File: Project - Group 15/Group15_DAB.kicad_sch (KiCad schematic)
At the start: 41 parts, among them J1 RJ45, J2 RJ45, J3 Power Header

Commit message: swag
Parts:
- FLT: value 100nF -> 22nF
- RIP: value 100nF -> 1nF
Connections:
- new net: R11., R15., R17., U4.2 (IN+)
- new net: R10., R14., R16., U4.3 (IN-)
- new net: R13., R2., R5., U3.3 (IN-)
- new net: R1., R12., R6., U3.2 (IN+)
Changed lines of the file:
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@@
 	)
 	(symbol
-		(lib_name "491_Symbols:RES_1k_805_PAN")
 		(lib_id "491_Symbols:RES_1k_805_PAN")
 		(at 87.63 39.37 270)
@@
 	)
 	(symbol
-		(lib_name "491_Symbols:RES_1k_805_PAN")
 		(lib_id "491_Symbols:RES_1k_805_PAN")
 		(at 53.34 26.67 270)
@@
 	)
 	(symbol
-		(lib_name "491_Symbols:RES_1k_805_PAN")
 		(lib_id "491_Symbols:RES_1k_805_PAN")
 		(at 198.12 118.11 0)
@@
 	)
 	(symbol
-		(lib_name "491_Symbols:RES_1k_805_PAN")
 		(lib_id "491_Symbols:RES_1k_805_PAN")
 		(at 229.87 140.97 0)
@@
 	)
 	(symbol
-		(lib_name "491_Symbols:RES_1k_805_PAN")
 		(lib_id "491_Symbols:RES_1k_805_PAN")
 		(at 142.24 149.86 0)
@@
 	)
 	(symbol
-		(lib_name "491_Symbols:RES_1k_805_PAN")
 		(lib_id "491_Symbols:RES_1k_805_PAN")
 		(at 198.12 128.27 0)
@@
 	)
 	(symbol
-		(lib_name "491_Symbols:RES_1k_805_PAN")
 		(lib_id "491_Symbols:RES_1k_805_PAN")
 		(at 142.24 95.25 0)
@@
 	)
 	(symbol
-		(lib_name "491_Symbols:RES_1k_805_PAN")
 		(lib_id "491_Symbols:RES_1k_805_PAN")
 		(at 231.14 95.25 0)
@@
 	)
 	(symbol
-		(lib_name "491_Symbols:RES_1k_805_PAN")
 		(lib_id "491_Symbols:RES_1k_805_PAN")
 		(at 66.04 26.67 270)
@@
 	)
 	(symbol
-		(lib_name "491_Symbols:RES_1k_805_PAN")
 		(lib_id "491_Symbols:RES_1k_805_PAN")
 		(at 107.95 128.27 0)
@@
 	)
 	(symbol
-		(lib_name "491_Symbols:RES_1k_805_PAN")
 		(lib_id "491_Symbols:RES_1k_805_PAN")
 		(at 142.24 86.36 0)
@@
 	)
 	(symbol
-		(lib_name "491_Symbols:RES_1k_805_PAN")
 		(lib_id "491_Symbols:RES_1k_805_PAN")
 		(at 87.63 26.67 270)
@@
 			)
 		)
-		(property "Value" "100nF"
+		(property "Value" "1nF"
 			(at 173.228 59.436 90)
 			(effects
@@
 	)
 	(symbol
-		(lib_name "491_Symbols:RES_47k_805_PAN")
 		(lib_id "491_Symbols:RES_47k_805_PAN")
 		(at 238.76 44.45 0)
@@
 		)
 		(property "Value" "3k"
-			(at 190.246 66.802 0)
+			(at 190.754 67.056 90)
 			(effects
 				(font
@@
 	)
 	(symbol
-		(lib_name "491_Symbols:RES_1k_805_PAN")
 		(lib_id "491_Symbols:RES_1k_805_PAN")
 		(at 107.95 118.11 0)
@@
 			)
 		)
-		(property "Value" "100nF"
+		(property "Value" "22nF"
 			(at 185.674 56.896 90)
 			(effects
@@
 	)
 	(symbol
-		(lib_name "491_Symbols:RES_1k_805_PAN")
 		(lib_id "491_Symbols:RES_1k_805_PAN")
 		(at 229.87 149.86 0)
@@
 	)
 	(symbol
-		(lib_name "491_Symbols:RES_1k_805_PAN")
 		(lib_id "491_Symbols:RES_1k_805_PAN")
 		(at 231.14 86.36 0)
@@
 	)
 	(symbol
-		(lib_name "491_Symbols:RES_1k_805_PAN")
 		(lib_id "491_Symbols:RES_1k_805_PAN")
 		(at 142.24 140.97 0)

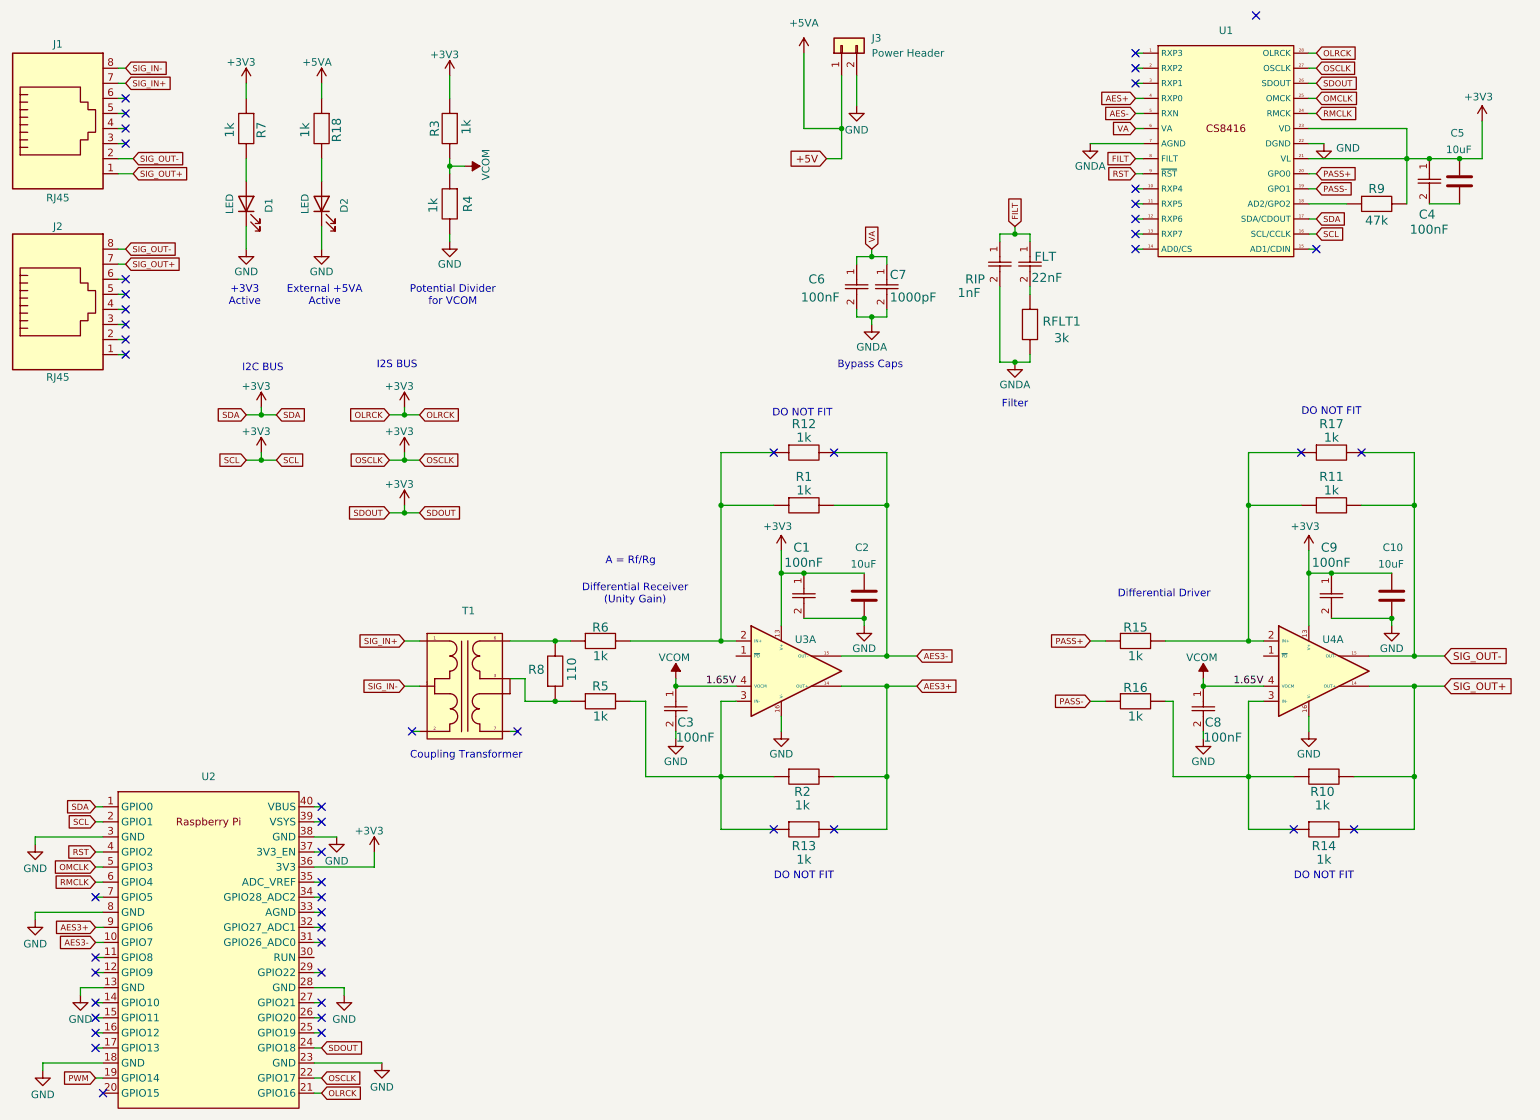
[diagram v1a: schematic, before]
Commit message: Lab Jordan Reviewed kinda
Pls add pull up resistors!!!!
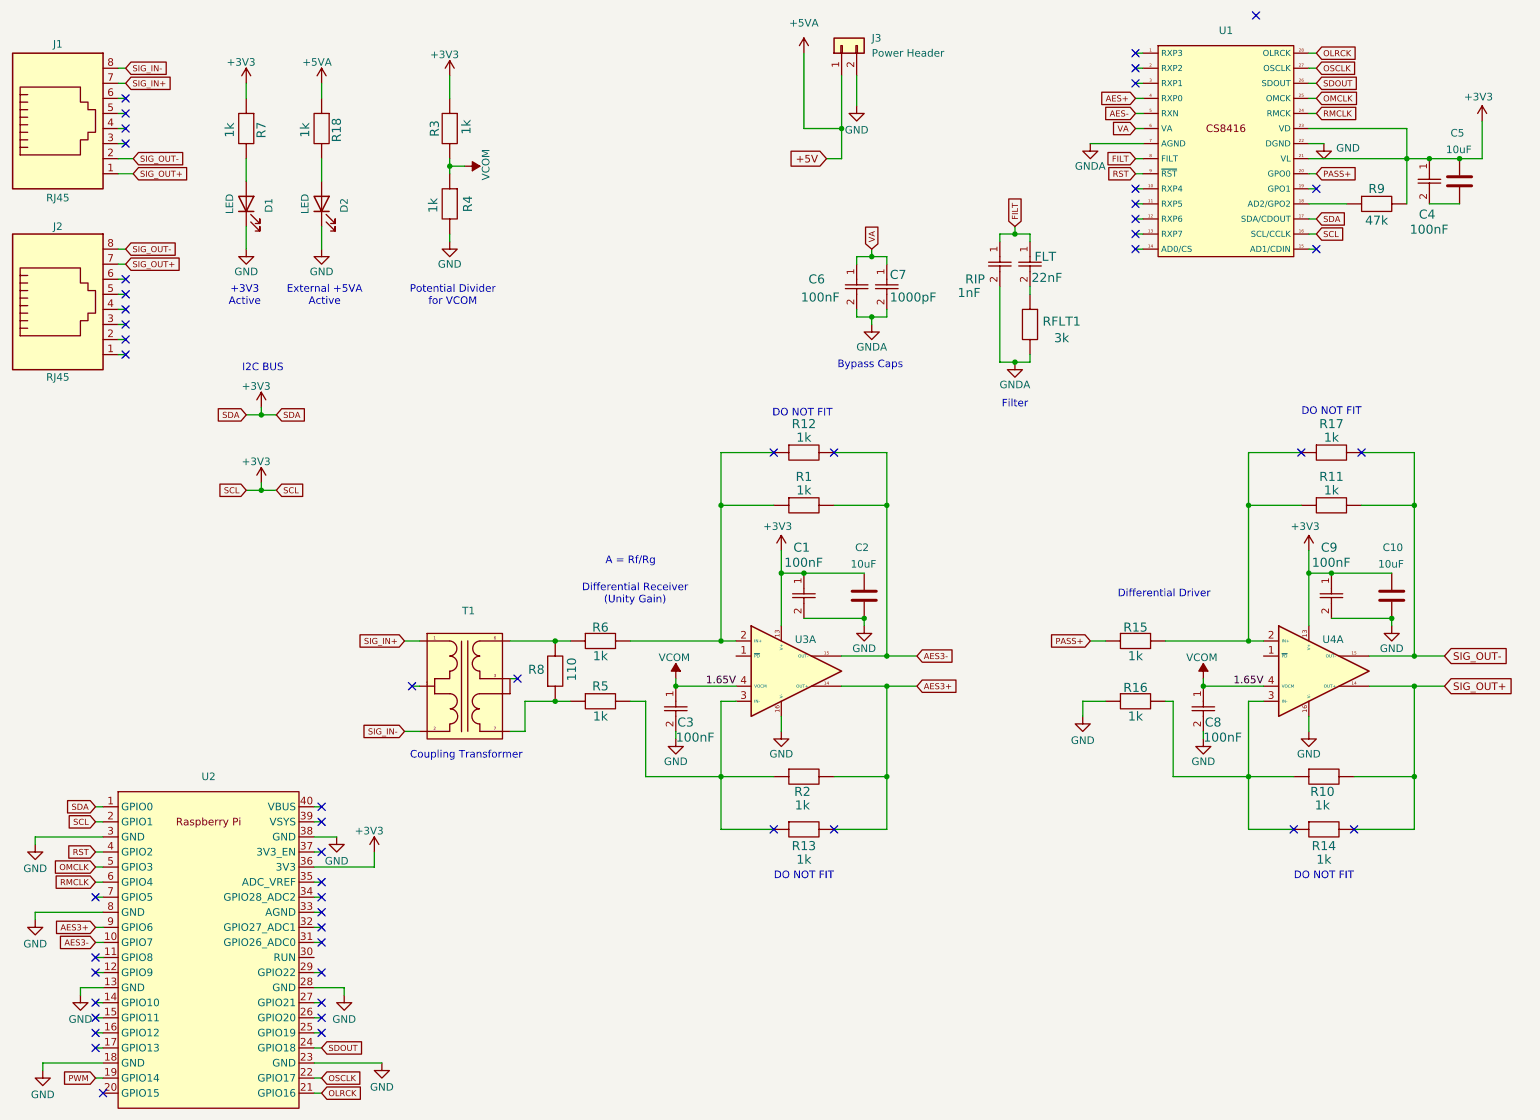
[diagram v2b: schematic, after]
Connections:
- net +3V3: no longer U1.26 (SDOUT), U1.27 (OSCLK), U1.28 (OLRCK), U2.21 (GPIO16), U2.22 (GPIO17), U2.24 (GPIO18)
- net GND: now also R16.
- net SIG_IN-: now also T1.2; no longer T1.5
- net at T1.7: now also R5., R8.
- net PASS-: no longer names the net of U1.19 (GPO1)
- net PASS-: no longer R16.
- new net: R11., R15., R17., U4.2 (IN+)
- new net: R10., R14., R16., U4.3 (IN-)
- new net: R13., R2., R5., U3.3 (IN-)
- new net: R1., R12., R6., U3.2 (IN+)
- new net OLRCK: U1.28 (OLRCK), U2.21 (GPIO16)
- new net OSCLK: U1.27 (OSCLK), U2.22 (GPIO17)
- new net SDOUT: U1.26 (SDOUT), U2.24 (GPIO18)
- now unconnected: T1.3
- no-connect marks 50 -> 51
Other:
- note removed: "I2S BUS"

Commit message: Swag
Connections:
- net +3V3: no longer U1.16 (SCL/CCLK), U2.2 (GPIO1)
- new net: R11., R15., R17., U4.2 (IN+)
- new net: R10., R14., R16., U4.3 (IN-)
- new net: R13., R2., R5., U3.3 (IN-)
- new net: R1., R12., R6., U3.2 (IN+)
- new net SCL: U1.16 (SCL/CCLK), U2.2 (GPIO1)
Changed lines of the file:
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@@
 	)
 	(junction
-		(at 55.88 92.71)
+		(at 55.88 104.14)
 		(diameter 0)
 		(color 0 0 0 0)
@@
 	(wire
 		(pts
-			(xy 53.34 92.71) (xy 55.88 92.71)
+			(xy 53.34 104.14) (xy 55.88 104.14)
 		)
 		(stroke
@@
 	(wire
 		(pts
-			(xy 55.88 92.71) (xy 58.42 92.71)
+			(xy 55.88 104.14) (xy 58.42 104.14)
 		)
 		(stroke
@@
 	(wire
 		(pts
-			(xy 55.88 91.44) (xy 55.88 92.71)
+			(xy 55.88 102.87) (xy 55.88 104.14)
 		)
 		(stroke
@@
 	(global_label "SCL"
 		(shape input)
-		(at 58.42 92.71 0)
+		(at 58.42 104.14 0)
 		(fields_autoplaced yes)
 		(effects
@@
 		)
 		(property "Intersheetrefs" "${INTERSHEET_REFS}"
-			(at 63.614 92.71 0)
+			(at 63.614 104.14 0)
 			(effects
 				(font
@@
 	(global_label "SCL"
 		(shape input)
-		(at 53.34 92.71 180)
+		(at 53.34 104.14 180)
 		(fields_autoplaced yes)
 		(effects
@@
 		)
 		(property "Intersheetrefs" "${INTERSHEET_REFS}"
-			(at 48.146 92.71 0)
+			(at 48.146 104.14 0)
 			(effects
 				(font
@@
 	)
 	(symbol
+		(lib_id "power:+3V3")
+		(at 55.88 95.25 0)
+		(unit 1)
+		(exclude_from_sim no)
+		(in_bom yes)
+		(on_board yes)
+		(dnp no)
+		(property "Reference" "MCU_PWR07"
+			(at 55.88 99.06 0)
+			(effects
+				(font
+					(size 1.27 1.27)
+				)
+				(hide yes)
+			)
+		)
+		(property "Value" "+3V3"
+			(at 52.578 91.694 0)
+			(effects
+				(font
+					(size 1.27 1.27)
+				)
+				(justify left)
+			)
+		)
+		(property "Footprint" ""
+			(at 55.88 95.25 0)
+			(effects
+				(font
+					(size 1.27 1.27)
+				)
+				(hide yes)
+			)
+		)
+		(property "Datasheet" ""
+			(at 55.88 95.25 0)
+			(effects
+				(font
+					(size 1.27 1.27)
+				)
+				(hide yes)
+			)
+		)
+		(property "Description" "Power symbol creates a global label with name \"+3V3\""
+			(at 55.88 95.25 0)
+			(effects
+				(font
+					(size 1.27 1.27)
+				)
+				(hide yes)
+			)
+		)
+		(pin "1"
+		)
+		(instances
+			(project "Group15_DAB"
+				(path "/43b85bcc-c949-42f4-ac7f-1cc8aa66ccee"
+					(reference "MCU_PWR07")
+					(unit 1)
+				)
+			)
+		)
+	)
+	(symbol
 		(lib_id "power:GND")
 		(at 214.63 134.62 0)
@@
 	)
 	(symbol
-		(lib_id "power:+3V3")
-		(at 55.88 91.44 0)
-		(unit 1)
-		(exclude_from_sim no)
-		(in_bom yes)
-		(on_board yes)
-		(dnp no)
-		(property "Reference" "MCU_PWR07"
-			(at 55.88 95.25 0)
-			(effects
-				(font
-					(size 1.27 1.27)
-				)
-				(hide yes)
-			)
-		)
-		(property "Value" "+3V3"
-			(at 52.578 87.884 0)
-			(effects
-				(font
-					(size 1.27 1.27)
-				)
-				(justify left)
-			)
-		)
-		(property "Footprint" ""
-			(at 55.88 91.44 0)
-			(effects
-				(font
-					(size 1.27 1.27)
-				)
-				(hide yes)
-			)
-		)
-		(property "Datasheet" ""
-			(at 55.88 91.44 0)
-			(effects
-				(font
-					(size 1.27 1.27)
-				)
-				(hide yes)
-			)
-		)
-		(property "Description" "Power symbol creates a global label with name \"+3V3\""
-			(at 55.88 91.44 0)
-			(effects
-				(font
-					(size 1.27 1.27)
-				)
-				(hide yes)
-			)
-		)
-		(pin "1"
-		)
-		(instances
-			(project "Group15_DAB"
-				(path "/43b85bcc-c949-42f4-ac7f-1cc8aa66ccee"
-					(reference "MCU_PWR07")
-					(unit 1)
-				)
-			)
-		)
-	)
-	(symbol
 		(lib_id "power:GND")
 		(at 143.51 133.35 0)
@@
 	)
 	(symbol
+		(lib_name "491_Symbols:RES_1k_805_PAN")
 		(lib_id "491_Symbols:RES_1k_805_PAN")
 		(at 231.14 86.36 0)
@@
 		(dnp no)
 		(property "Reference" "R17"
-			(at 236.22 81.534 0)
+			(at 235.966 81.788 0)
 			(effects
 				(font

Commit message: Darren
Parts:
- added R19, R20: 1k, 491_Footprints:RES_1k_805_PAN, symbol 491_Symbols:RES_1k_805_PAN
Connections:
- net +3V3: now also R19., R20.; no longer U1.17 (SDA/CDOUT), U2.1 (GPIO0)
- net SCL: now also R19.
- new net: R11., R15., R17., U4.2 (IN+)
- new net: R10., R14., R16., U4.3 (IN-)
- new net: R13., R2., R5., U3.3 (IN-)
- new net: R1., R12., R6., U3.2 (IN+)
- new net SDA: R20., U1.17 (SDA/CDOUT), U2.1 (GPIO0)
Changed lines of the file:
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@@
 	)
 	(junction
-		(at 55.88 80.01)
-		(diameter 0)
-		(color 0 0 0 0)
-	)
-	(junction
 		(at 236.22 106.68)
 		(diameter 0)
@@
 	)
 	(junction
+		(at 73.66 104.14)
+		(diameter 0)
+		(color 0 0 0 0)
+	)
+	(junction
 		(at 182.88 71.12)
 		(diameter 0)
@@
 	(wire
 		(pts
+			(xy 73.66 104.14) (xy 76.2 104.14)
+		)
+		(stroke
+			(width 0)
+			(type default)
+		)
+	)
+	(wire
+		(pts
 			(xy 97.79 118.11) (xy 105.41 118.11)
 		)
@@
 	(wire
 		(pts
-			(xy 55.88 78.74) (xy 55.88 80.01)
-		)
-		(stroke
-			(width 0)
-			(type default)
-		)
-	)
-	(wire
-		(pts
-			(xy 55.88 80.01) (xy 53.34 80.01)
-		)
-		(stroke
-			(width 0)
-			(type default)
-		)
-	)
-	(wire
-		(pts
 			(xy 64.77 156.21) (xy 74.93 156.21)
 		)
@@
 	(wire
 		(pts
+			(xy 73.66 90.17) (xy 73.66 91.44)
+		)
+		(stroke
+			(width 0)
+			(type default)
+		)
+	)
+	(wire
+		(pts
 			(xy 153.67 125.73) (xy 161.29 125.73)
 		)
@@
 	(wire
 		(pts
+			(xy 73.66 104.14) (xy 71.12 104.14)
+		)
+		(stroke
+			(width 0)
+			(type default)
+		)
+	)
+	(wire
+		(pts
 			(xy 33.02 26.67) (xy 31.75 26.67)
 		)
@@
 	(wire
 		(pts
+			(xy 55.88 91.44) (xy 55.88 90.17)
+		)
+		(stroke
+			(width 0)
+			(type default)
+		)
+	)
+	(wire
+		(pts
 			(xy 233.68 46.99) (xy 232.41 46.99)
 		)
@@
 	(wire
 		(pts
+			(xy 73.66 101.6) (xy 73.66 104.14)
+		)
+		(stroke
+			(width 0)
+			(type default)
+		)
+	)
+	(wire
+		(pts
 			(xy 80.01 118.11) (xy 82.55 118.11)
 		)
@@
 	(wire
 		(pts
-			(xy 55.88 102.87) (xy 55.88 104.14)
+			(xy 55.88 101.6) (xy 55.88 104.14)
 		)
 		(stroke
@@
 	(wire
 		(pts
-			(xy 55.88 80.01) (xy 58.42 80.01)
-		)
-		(stroke
-			(width 0)
-			(type default)
-		)
-	)
-	(wire
-		(pts
 			(xy 242.57 125.73) (xy 250.19 125.73)
 		)
@@
 		)
 	)
+	(global_label "SDA"
+		(shape input)
+		(at 71.12 104.14 180)
+		(fields_autoplaced yes)
+		(effects
+			(font
+				(size 1.016 1.016)
+			)
+			(justify right)
+		)
+		(property "Intersheetrefs" "${INTERSHEET_REFS}"
+			(at 65.8776 104.14 0)
+			(effects
+				(font
+					(size 1.27 1.27)
+				)
+				(justify right)
+				(hide yes)
+			)
+		)
+	)
 	(global_label "SDOUT"
 		(shape input)
@@
 	(global_label "SDA"
 		(shape input)
-		(at 58.42 80.01 0)
+		(at 76.2 104.14 0)
 		(fields_autoplaced yes)
 		(effects
@@
 		)
 		(property "Intersheetrefs" "${INTERSHEET_REFS}"
-			(at 63.6624 80.01 0)
+			(at 81.4424 104.14 0)
 			(effects
 				(font
@@
 		)
 	)
-	(global_label "SDA"
-		(shape input)
-		(at 53.34 80.01 180)
-		(fields_autoplaced yes)
-		(effects
-			(font
-				(size 1.016 1.016)
-			)
-			(justify right)
-		)
-		(property "Intersheetrefs" "${INTERSHEET_REFS}"
-			(at 48.0976 80.01 0)
-			(effects
-				(font
-					(size 1.27 1.27)
-				)
-				(justify right)
-				(hide yes)
-			)
-		)
-	)
 	(symbol
 		(lib_id "power:GND")
@@
 	)
 	(symbol
+		(lib_name "491_Symbols:RES_1k_805_PAN")
+		(lib_id "491_Symbols:RES_1k_805_PAN")
+		(at 73.66 91.44 270)
+		(unit 1)
+		(exclude_from_sim no)
+		(in_bom yes)
+		(on_board yes)
+		(dnp no)
+		(property "Reference" "R20"
+			(at 78.486 96.52 0)
+			(effects
+				(font
+					(size 1.524 1.524)
+				)
+			)
+		)
+		(property "Value" "1k"
+			(at 76.2 96.52 0)
+			(effects
+				(font
+					(size 1.524 1.524)
+				)
+			)
+		)
+		(property "Footprint" "491_Footprints:RES_1k_805_PAN"
+			(at 65.532 99.314 0)
+			(effects
+				(font
+					(size 1.27 1.27)
+					(italic yes)
+				)
+				(hide yes)
+			)
+		)
+		(property "Datasheet" "ERJ-2RKF1001X"
+			(at 63.754 99.568 0)
+			(effects
+				(font
+					(size 1.27 1.27)
+					(italic yes)
+				)
+				(hide yes)
+			)
+		)
+		(property "Description" ""
+			(at 73.66 91.44 0)
+			(effects
+				(font
+					(size 1.27 1.27)
+				)
+				(hide yes)
+			)
+		)
+		(pin ""
+		)
+		(pin ""
+		)
+		(instances
+			(project "Group15_DAB"
+				(path "/43b85bcc-c949-42f4-ac7f-1cc8aa66ccee"
+					(reference "R20")
+					(unit 1)
+				)
+			)
+		)
+	)
+	(symbol
 		(lib_id "power:GND")
 		(at 66.04 52.07 0)
@@
 	(symbol
 		(lib_id "power:+3V3")
-		(at 55.88 95.25 0)
+		(at 55.88 90.17 0)
 		(unit 1)
 		(exclude_from_sim no)
@@
 		(dnp no)
 		(property "Reference" "MCU_PWR07"
-			(at 55.88 99.06 0)
+			(at 55.88 93.98 0)
 			(effects
 				(font
@@
 		)
 		(property "Value" "+3V3"
-			(at 52.578 91.694 0)
+			(at 52.578 86.614 0)
 			(effects
 				(font
@@
 		)
 		(property "Footprint" ""
-			(at 55.88 95.25 0)
+			(at 55.88 90.17 0)
 			(effects
 				(font
@@
 		)
 		(property "Datasheet" ""
-			(at 55.88 95.25 0)
+			(at 55.88 90.17 0)
 			(effects
 				(font
@@
 		)
 		(property "Description" "Power symbol creates a global label with name \"+3V3\""
-			(at 55.88 95.25 0)
+			(at 55.88 90.17 0)
 			(effects
 				(font
@@
 	(symbol
 		(lib_id "power:+3V3")
-		(at 55.88 78.74 0)
+		(at 73.66 90.17 0)
 		(unit 1)
 		(exclude_from_sim no)
@@
 		(dnp no)
 		(property "Reference" "MCU_PWR05"
-			(at 55.88 82.55 0)
+			(at 73.66 93.98 0)
 			(effects
 				(font
@@
 		)
 		(property "Value" "+3V3"
-			(at 52.578 75.184 0)
+			(at 70.358 86.614 0)
 			(effects
 				(font
@@
 		)
 		(property "Footprint" ""
-			(at 55.88 78.74 0)
+			(at 73.66 90.17 0)
 			(effects
 				(font
@@
 		)
 		(property "Datasheet" ""
-			(at 55.88 78.74 0)
+			(at 73.66 90.17 0)
 			(effects
 				(font
@@
 		)
 		(property "Description" "Power symbol creates a global label with name \"+3V3\""
-			(at 55.88 78.74 0)
+			(at 73.66 90.17 0)
 			(effects
 				(font
@@
 	)
 	(symbol
-		(lib_name "491_Symbols:RES_1k_805_PAN")
 		(lib_id "491_Symbols:RES_1k_805_PAN")
 		(at 231.14 86.36 0)
@@
 					(unit 1)
 				)
+			)
+		)
+	)
+	(symbol
+		(lib_name "491_Symbols:RES_1k_805_PAN")
+		(lib_id "491_Symbols:RES_1k_805_PAN")
+		(at 55.88 91.44 270)
+		(unit 1)
+		(exclude_from_sim no)
+		(in_bom yes)
+		(on_board yes)
+		(dnp no)
+		(property "Reference" "R19"
+			(at 60.706 96.52 0)
+			(effects
+				(font
+					(size 1.524 1.524)
+				)
+			)
+		)
+		(property "Value" "1k"
+			(at 58.42 96.52 0)
+			(effects
+				(font
+					(size 1.524 1.524)
+				)
+			)
+		)
+		(property "Footprint" "491_Footprints:RES_1k_805_PAN"
+			(at 47.752 99.314 0)
+			(effects
+				(font
+					(size 1.27 1.27)
+					(italic yes)
+				)
+				(hide yes)
+			)
+		)
+		(property "Datasheet" "ERJ-2RKF1001X"
+			(at 45.974 99.568 0)
+			(effects
+				(font
+					(size 1.27 1.27)
+					(italic yes)
+				)
+				(hide yes)
+			)
+		)
+		(property "Description" ""
+			(at 55.88 91.44 0)
+			(effects
+				(font
+					(size 1.27 1.27)
+				)
+				(hide yes)
+			)
+		)
+		(pin ""
+		)
+		(pin ""
+		)
+		(instances
+			(project "Group15_DAB"
+				(path "/43b85bcc-c949-42f4-ac7f-1cc8aa66ccee"
+					(reference "R19")
+					(unit 1)
+				)
